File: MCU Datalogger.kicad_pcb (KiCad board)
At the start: 2 copper layers, 0 parts

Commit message: Setup Pcbnew
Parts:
- added BT1: Battery, Connector_PinHeader_1.00mm:PinHeader_1x02_P1.00mm_Vertical, F.Cu at (152.3, 95.1)
- added C1: 0.1uF, Capacitor_SMD:C_0805_2012Metric_Pad1.18x1.45mm_HandSolder, F.Cu at (148.2, 95.1)
- added C2: 22pF, Capacitor_SMD:C_0805_2012Metric_Pad1.18x1.45mm_HandSolder, F.Cu at (148.2, 98.1)
- added C3: 22pF, Capacitor_SMD:C_0805_2012Metric_Pad1.18x1.45mm_HandSolder, F.Cu at (148.2, 101.1)
- added C4: 0.1uF, Capacitor_SMD:C_0805_2012Metric_Pad1.18x1.45mm_HandSolder, F.Cu at (148.2, 104.1)
- added C5: 100nF, Capacitor_SMD:C_0805_2012Metric_Pad1.18x1.45mm_HandSolder, F.Cu at (148.2, 107.1)
- added D1: LED, LED_SMD:LED_0805_2012Metric_Pad1.15x1.40mm_HandSolder, F.Cu at (125.5, 104.6)
- added D2: LED, LED_SMD:LED_0805_2012Metric_Pad1.15x1.40mm_HandSolder, F.Cu at (125.5, 107.6)
- added H1: MountingHole, MountingHole:MountingHole_2.1mm, F.Cu at (126.0, 82.9)
- added H2: MountingHole, MountingHole:MountingHole_2.1mm, F.Cu at (126.0, 88.7)
- added H3: MountingHole, MountingHole:MountingHole_2.1mm, F.Cu at (126.0, 94.4)
- added H4: MountingHole, MountingHole:MountingHole_2.1mm, F.Cu at (126.0, 100.2)
- added J1: Conn_01x09_Pin, Connector_PinHeader_2.54mm:PinHeader_1x09_P2.54mm_Vertical, F.Cu at (158.5, 82.4)
- added J2: Conn_01x04_Pin, Connector_PinHeader_2.54mm:PinHeader_1x04_P2.54mm_Vertical, F.Cu at (163.2, 82.4)
- added J3: Conn_02x03_Odd_Even, Connector_PinHeader_2.54mm:PinHeader_2x03_P2.54mm_Vertical, F.Cu at (163.2, 94.6)
- added J4: Conn_01x04_Pin, Connector_PinHeader_2.54mm:PinHeader_1x04_P2.54mm_Vertical, F.Cu at (167.8, 82.4)
- added R1: 10k, Resistor_SMD:R_0805_2012Metric_Pad1.20x1.40mm_HandSolder, F.Cu at (131.2, 81.5)
- added R2: 10k, Resistor_SMD:R_0805_2012Metric_Pad1.20x1.40mm_HandSolder, F.Cu at (131.2, 84.5)
- added R3: 4.7k, Resistor_SMD:R_0805_2012Metric_Pad1.20x1.40mm_HandSolder, F.Cu at (131.2, 87.4)
- added R4: 4.7k, Resistor_SMD:R_0805_2012Metric_Pad1.20x1.40mm_HandSolder, F.Cu at (131.2, 90.4)
- added R5: 330, Resistor_SMD:R_0805_2012Metric_Pad1.20x1.40mm_HandSolder, F.Cu at (131.2, 93.3)
- added R6: 10k, Resistor_SMD:R_0805_2012Metric_Pad1.20x1.40mm_HandSolder, F.Cu at (131.2, 96.3)
- added R7: 330, Resistor_SMD:R_0805_2012Metric_Pad1.20x1.40mm_HandSolder, F.Cu at (131.2, 99.2)
- added U1: 24LC1025, Package_SO:SOIC-8_5.23x5.23mm_P1.27mm, F.Cu at (138.8, 83.4)
- added U2: DS1337S_, footprints:SOIC127P600X175-8N, F.Cu at (138.8, 108.2)
- added U3: 24LC1025, Package_SO:SOIC-8_5.23x5.23mm_P1.27mm, F.Cu at (138.8, 90.2)
- added U4: ATMEGA328P-AU, footprints:QFP80P900X900X120-32N, F.Cu at (140.2, 99.3)
- added Y1: 32.768 KHz, Crystal:Crystal_SMD_5032-2Pin_5.0x3.2mm_HandSoldering, F.Cu at (149.1, 82.5)
- added Y2: 16 MHz, Crystal:Crystal_SMD_5032-2Pin_5.0x3.2mm_HandSoldering, F.Cu at (149.1, 87.3)

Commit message: design change
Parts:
- moved H4 50.1 mm to (170.5, 123.2)
- moved J1 49.7 mm to (129.2, 122.6), turned to 90 degrees
- moved H2 45.6 mm to (170.5, 98.4)
- moved J4 42.7 mm to (153.6, 122.6), turned to 90 degrees
- moved Y1 39.4 mm to (126.0, 114.4), turned to 90 degrees
- moved R1 37.2 mm to (131.4, 118.7)
- moved D1 36.7 mm to (161.8, 99.1)
- moved R2 34.7 mm to (136.6, 118.7), turned to 180 degrees
- moved D2 33.0 mm to (157.4, 99.1)
- moved R4 32.6 mm to (157.4, 109.9)
- moved R6 32.1 mm to (161.8, 106.0)
- moved R3 32.1 mm to (157.4, 106.0), turned to 180 degrees
- moved R5 31.8 mm to (161.8, 102.2), turned to 180 degrees
- moved J2 30.3 mm to (167.3, 112.4)
- moved Y2 29.2 mm to (145.2, 116.2)
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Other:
- board outline added: 50.2 x 29.8 mm

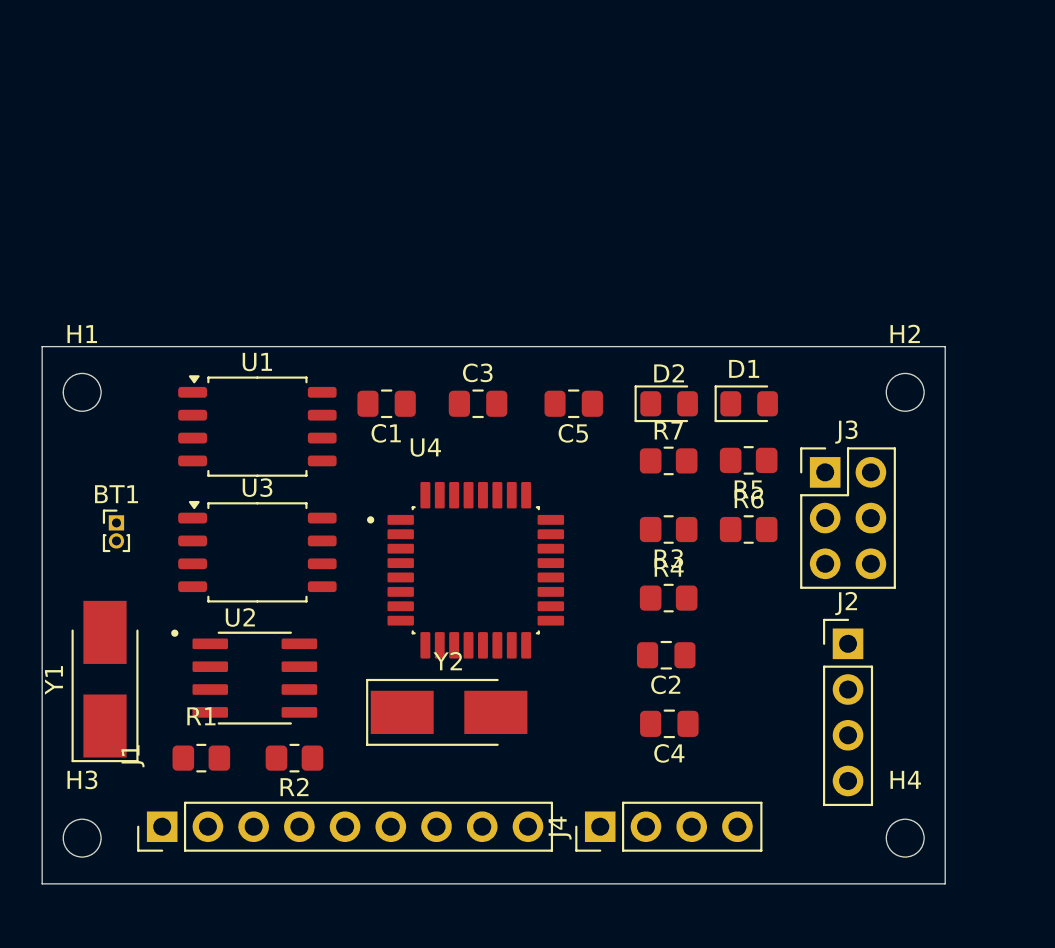
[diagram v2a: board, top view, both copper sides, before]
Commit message: Finished Routing PCB Tracks
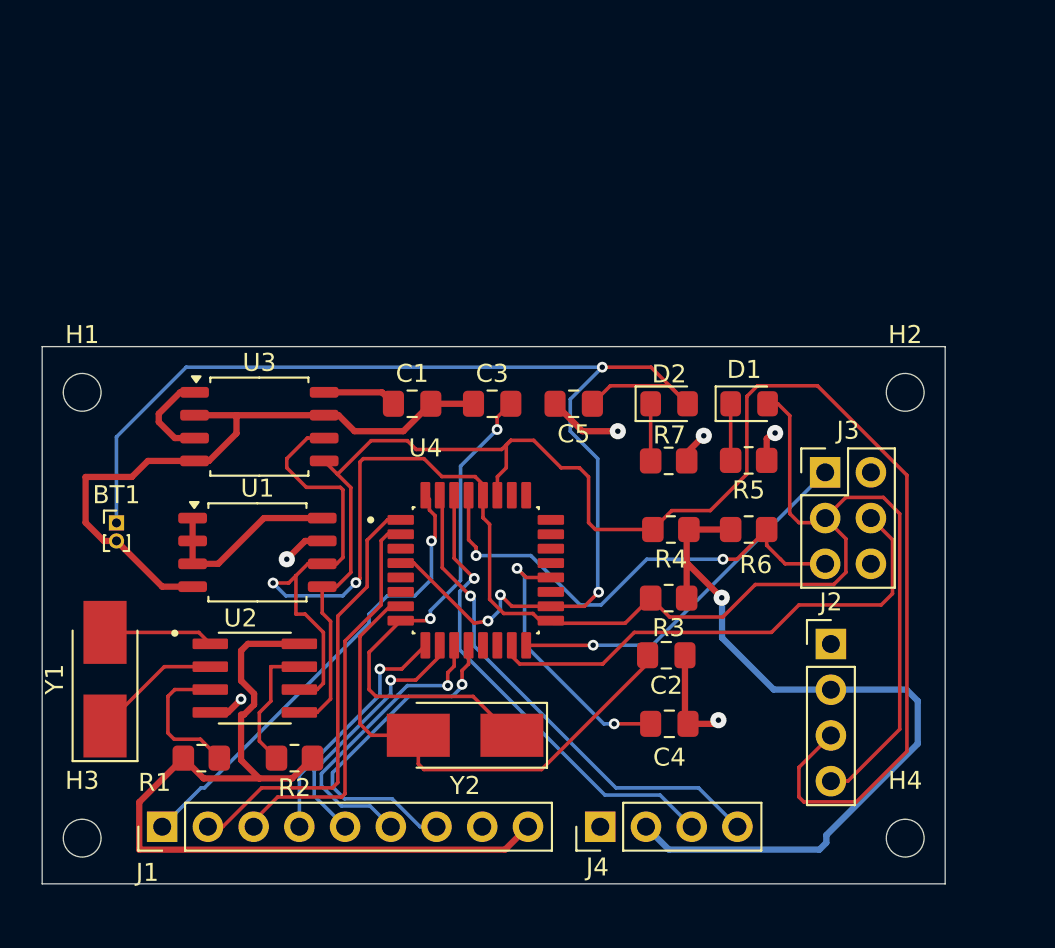
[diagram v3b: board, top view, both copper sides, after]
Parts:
- moved U3 6.99 mm to (134.6, 100.3)
- moved U1 6.98 mm to (134.5, 107.3)
- moved R4 3.81 mm to (157.5, 106.0), turned to 180 degrees
- moved R3 3.81 mm to (157.4, 109.9)
- moved Y2 1.55 mm to (146.1, 117.5), turned to 180 degrees
- moved C1 1.42 mm to (143.1, 99.1), turned to 0 degrees
- moved J2 0.95 mm to (166.4, 112.4)
- moved C3 0.78 mm to (147.6, 99.1)
- turned C4 to 0 degrees
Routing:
- net /Vcc: track 0.00 -> 112.3 mm, vias 0 -> 1
- net /SCL: track 0.00 -> 107.1 mm, vias 0 -> 2
- net /SDA: track 0.00 -> 91.6 mm
- net Net-(BT1-+): track 0.00 -> 73.1 mm, vias 0 -> 4
- net GND: track 0.00 -> 54.6 mm, vias 0 -> 6
- net Net-(U4-PB7): track 0.00 -> 29.4 mm, vias 0 -> 2
- net Net-(U4-PB6): track 0.00 -> 28.7 mm
- net /MOSI: track 0.00 -> 28.2 mm
- net /TX: track 0.00 -> 28.0 mm, vias 0 -> 1
- net /RESET: track 0.00 -> 27.1 mm, vias 0 -> 2
- net /RX: track 0.00 -> 26.3 mm, vias 0 -> 1
- net /D2: track 0.00 -> 25.9 mm, vias 0 -> 1
- net /D3: track 0.00 -> 24.7 mm
- net /D4: track 0.00 -> 22.1 mm
- net /MISO: track 0.00 -> 20.6 mm, vias 0 -> 1
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
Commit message: refined board outline
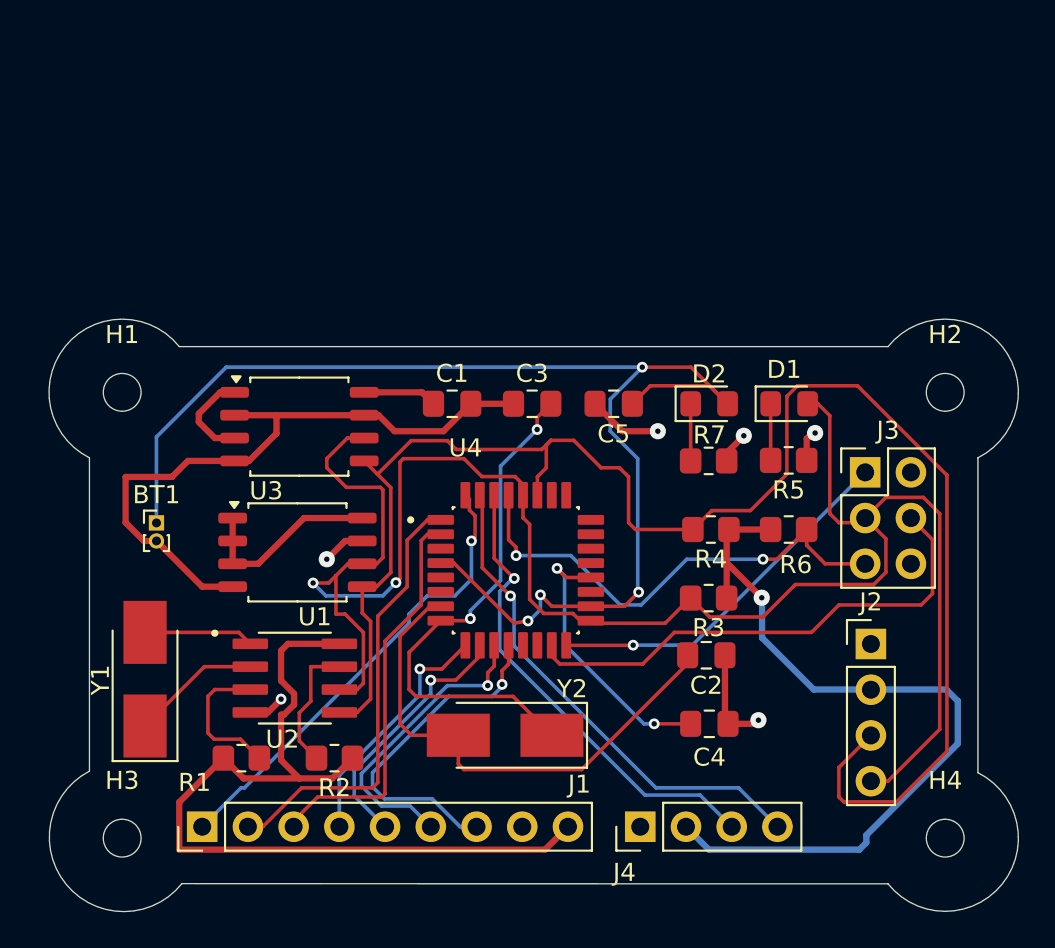
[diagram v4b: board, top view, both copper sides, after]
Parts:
- moved C1 2.22 mm to (145.3, 99.1)
- moved D1 2.22 mm to (164.1, 99.1)
- moved R3 2.22 mm to (159.6, 109.9)
- moved R7 2.22 mm to (159.6, 102.2)
- moved U1 2.22 mm to (136.7, 107.3)
- moved Y1 2.22 mm to (128.3, 114.4)
- moved BT1 2.22 mm to (128.9, 105.7)
- moved C2 2.22 mm to (159.4, 113.0)
- moved C3 2.22 mm to (149.8, 99.1)
- moved C4 2.22 mm to (159.6, 116.8)
- moved C5 2.22 mm to (154.3, 99.1)
- moved D2 2.22 mm to (159.6, 99.1)
- moved H1 2.22 mm to (127.0, 98.4)
- moved H2 2.22 mm to (172.7, 98.4)
- moved H3 2.22 mm to (127.0, 123.2)
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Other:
- board size 50.2 x 29.8 mm -> 53.8 x 32.9 mm

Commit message: Filled the GND zones
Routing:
- net GND: track 54.6 -> 73.6 mm, vias 6 -> 7
- net /SCL: track 107.1 -> 104.2 mm
- net /D2: track 25.9 -> 27.4 mm
- net /D4: track 22.1 -> 22.9 mm
- net /D3: track 24.7 -> 25.3 mm
- added copper zone on B.Cu, net GND

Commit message: Refined the tracks outline
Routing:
- net /Vcc: track 112.3 -> 160.6 mm, vias 1 -> 5
- net GND: track 73.6 -> 82.4 mm
- net /SDA: track 91.4 -> 89.9 mm
- net /SCL: track 104.2 -> 103.5 mm
- net Net-(BT1-+): track 73.1 -> 72.6 mm

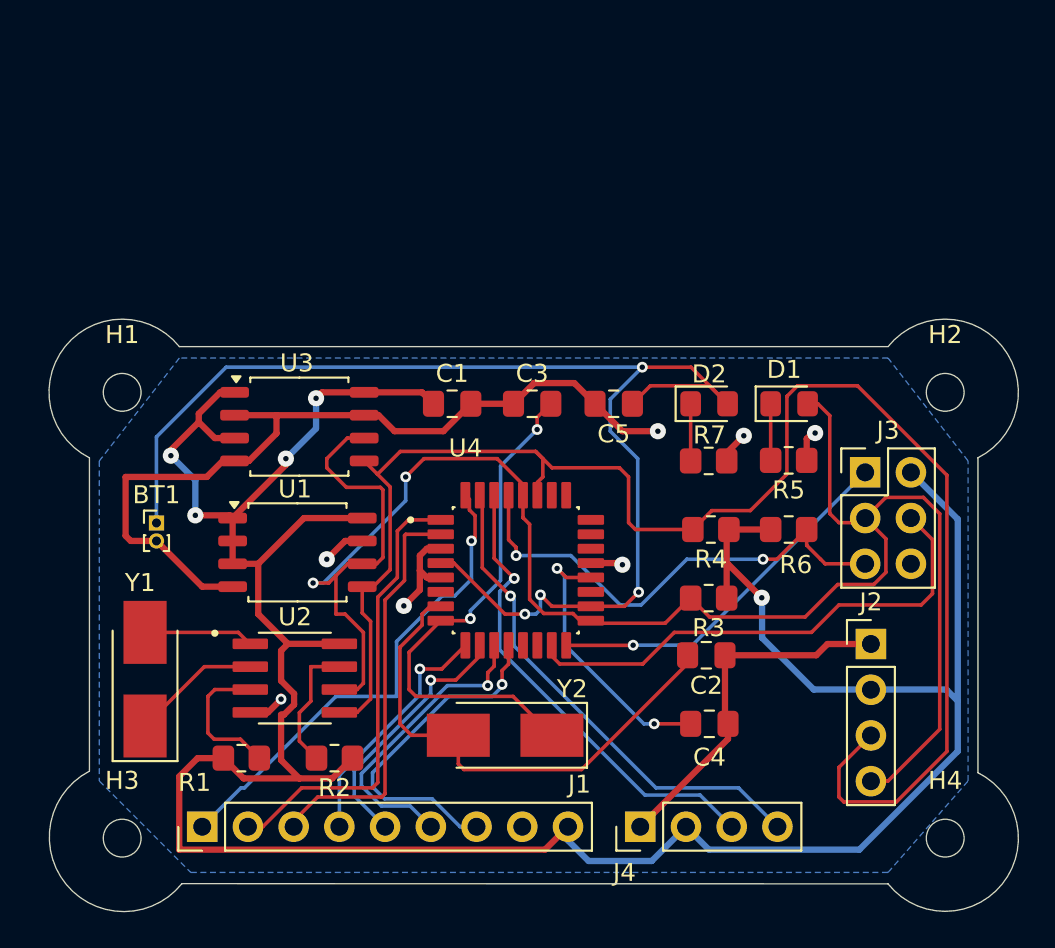
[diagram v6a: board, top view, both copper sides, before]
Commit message: Finished routing, silkscreen setup of the 2layer pcb
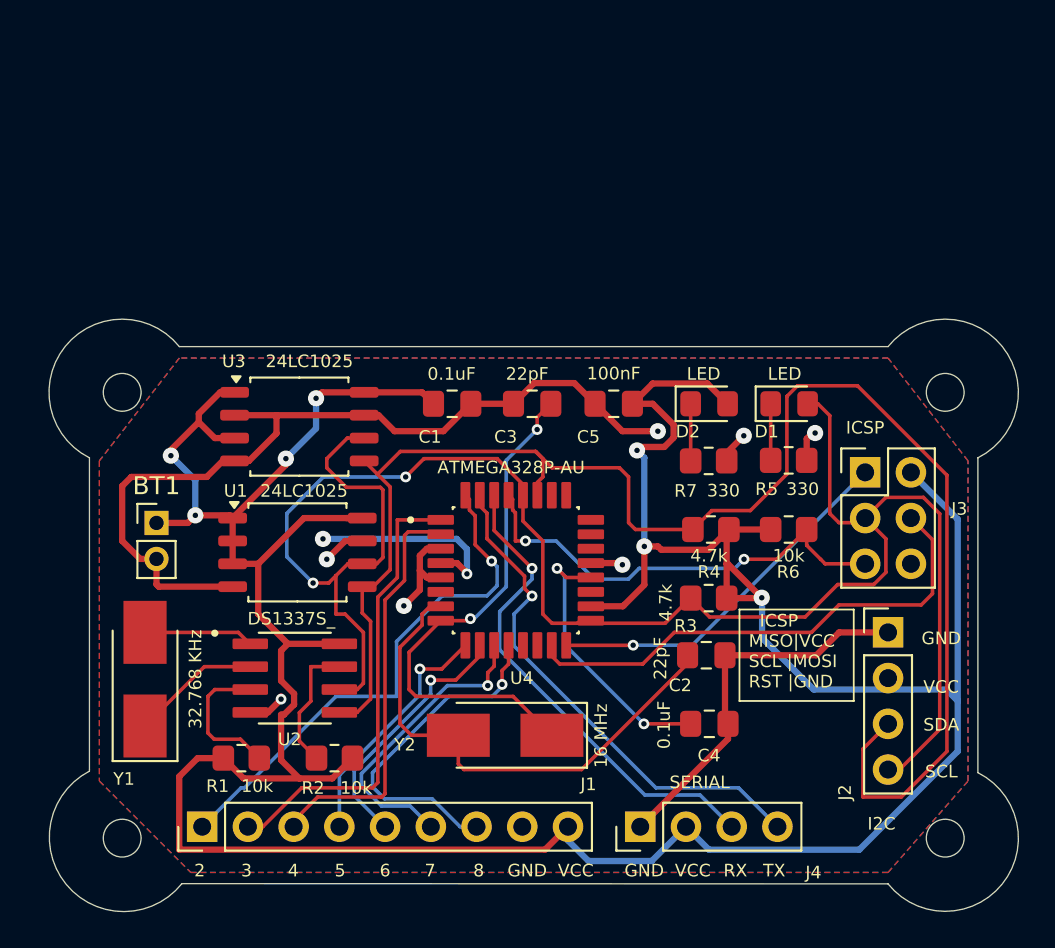
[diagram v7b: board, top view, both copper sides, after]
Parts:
- BT1: footprint Connector_PinHeader_1.00mm:PinHeader_1x02_P1.00mm_Vertical -> Connector_PinHeader_2.00mm:PinHeader_1x02_P2.00mm_Vertical
- moved J2 1.15 mm to (169.5, 111.8)
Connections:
- BT1 pad 1: Net-(BT1-+) -> /Vcc
- C5 pad 1: Net-(BT1-+) -> /Vcc
- D2 pad 2: Net-(BT1-+) -> /Vcc
- U4 pad 18: Net-(BT1-+) -> /Vcc
- U4 pad 4: Net-(BT1-+) -> /Vcc
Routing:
- net Net-(BT1-+): track 72.6 -> 0.00 mm, vias 4 -> 0
- net /Vcc: track 160.6 -> 205.6 mm, vias 5 -> 9
- net /SCL: track 103.5 -> 106.0 mm
- net GND: track 82.4 -> 84.7 mm
- net /D2: track 27.4 -> 29.5 mm
- net /RESET: track 27.1 -> 25.5 mm
- net /SDA: track 89.9 -> 88.8 mm
- net /TX: track 28.0 -> 28.8 mm
- net /RX: track 26.3 -> 27.2 mm
- added copper zone on F.Cu, net /Vcc
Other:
- board text added: "2"
- board text added: "3"
- board text added: "4"
- board text added: "5"
- board text added: "6"
- board text added: "7"
- board text added: "8"
- board text added: "GND"
- board text added: "I2C"
- board text added: "ICSP"
- board text added: "ICSP MISO|VCC SCL |MOSI RST |GND"
- board text added: "RX"
- board text added: "SCL"
- board text added: "SDA"
- board text added: "SERIAL"
- board text added: "TX"
- board text added: "VCC"
